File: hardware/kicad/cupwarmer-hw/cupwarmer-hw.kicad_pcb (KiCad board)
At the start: 4 copper layers, 56 x 56 mm, 50 parts, among them J1 I2C Service, J3 STATUS_MON, Q1 AO3400 SOT-23, U1 STWLC38JRM

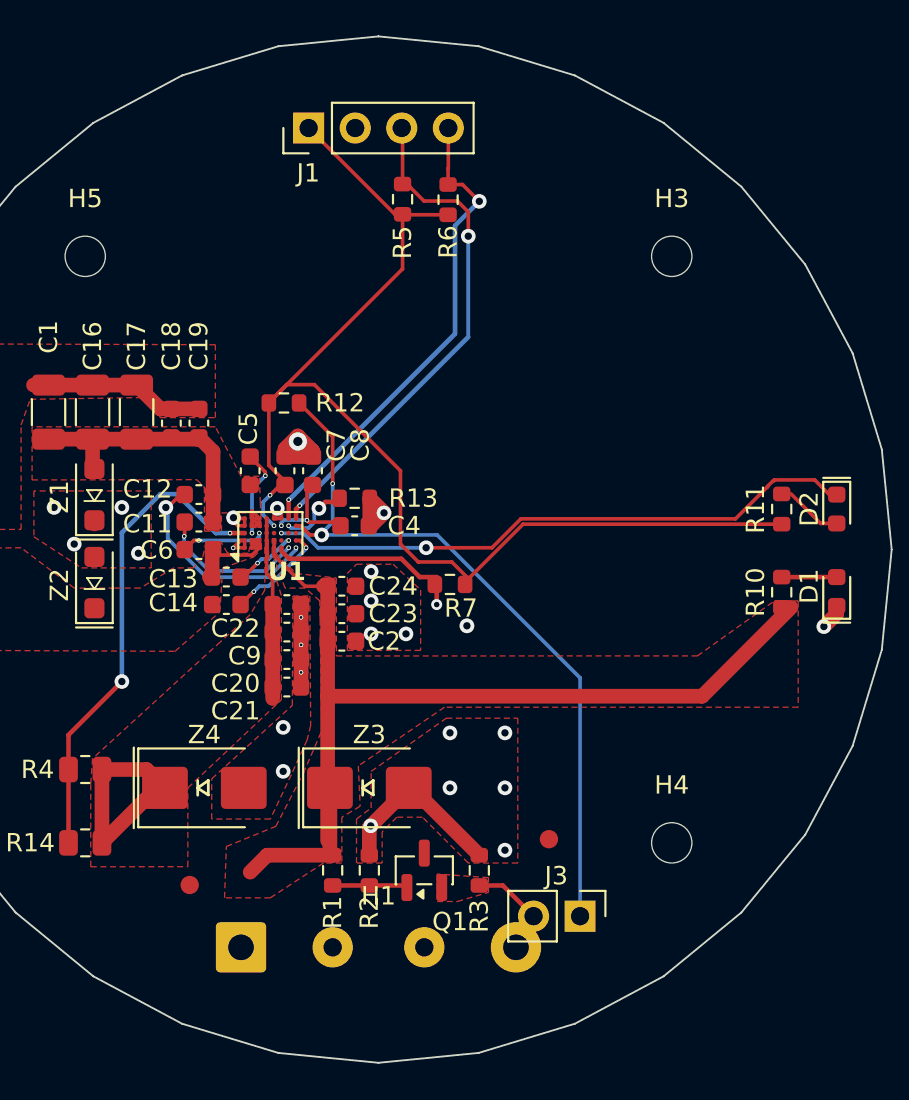
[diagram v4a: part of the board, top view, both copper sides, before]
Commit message: Refresh PCB footprint placements and TP1 land
Re-place and rotate several footprints (R1/R2/R3/R5/R6/R7, J1, H1, Q1)
to tidy reference text against the current layout, swap TP1 (TP_NTC)
from an SMD test pad to a 1x01 pin-header land for probe access, and
bump the default pad-mask drill/size in the project to 1.0/1.7 mm.

Co-Authored-By: Claude Opus 4.7 (1M context) <noreply@anthropic.com>
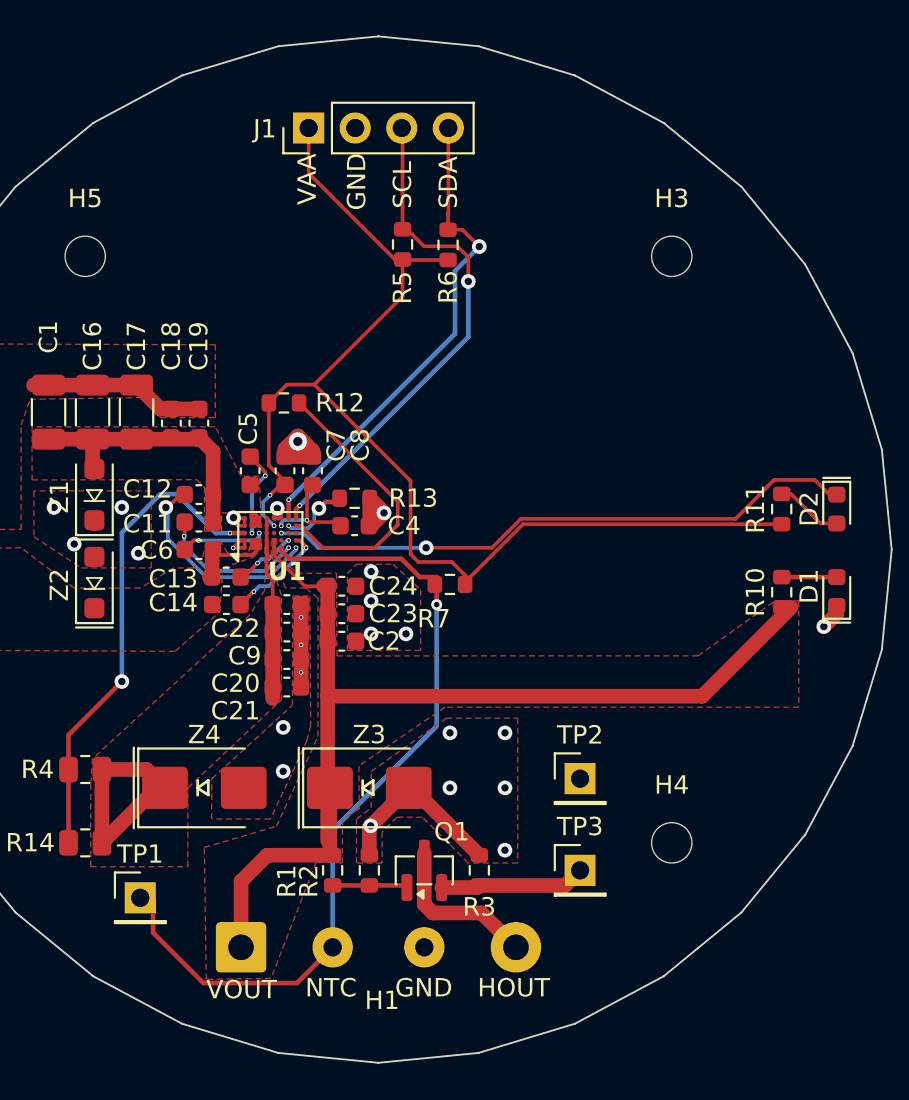
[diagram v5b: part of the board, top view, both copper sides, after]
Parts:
- removed J3: STATUS_MON, Connector_PinHeader_2.54mm:PinHeader_1x02_P2.54mm_Vertical
- added TP3: TP_I_HEATER_MON, Connector_PinHeader_2.54mm:PinHeader_1x01_P2.54mm_Vertical, F.Cu at (111.0, 117.5)
- TP1, TP2: footprint cupwarmer:TestPoint_Pad_D1.0mm_NoSilk -> Connector_PinHeader_2.54mm:PinHeader_1x01_P2.54mm_Vertical
- moved TP2 3.71 mm to (111.0, 112.5)
- moved TP1 2.79 mm to (87.0, 119.0)
- moved R5 2.47 mm to (101.3, 83.4)
- moved R6 2.47 mm to (103.8, 83.4)
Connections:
- net RX_INTB renamed Net-(U1-INTB)
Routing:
- net RX_NTC: track 10.7 -> 45.3 mm
- net Net-(U1-INTB): track 40.3 -> 15.6 mm, vias 2 -> 0
- net /heater-control/HEATER_OUT: track 0.00 -> 8.77 mm
- net VOUT_12V: track 55.1 -> 59.4 mm
- net I_HEATER_MON: track 3.99 -> 8.12 mm
- net RX_VAA: track 67.1 -> 65.1 mm, vias 3 -> 2
- removed copper zone on F.Cu, net I_HEATER_MON
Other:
- board text added: "GND"
- board text added: "HOUT"
- board text added: "NTC"
- board text added: "SCL"
- board text added: "SDA"
- board text added: "VAA"
- board text added: "VOUT"

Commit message: Add B.Cu SYS_GND pour and exclude H1/L1 wire pads from BOM/POS
- Add SYS_GND zone to B.Cu (full board polygon, fill params matching
  In1.Cu/In2.Cu GND pours) so the back-side signal layer carries a GND
  plane for return currents and EMI shielding.
- Mark H1 (heater harness) and L1 (Wuerth coil) as
  exclude_from_pos_files / exclude_from_bom in both the PCB instances
  and the cupwarmer.pretty library footprints. They are hand-soldered
  wire pads and should not appear in JLCPCB Pick&Place / BOM outputs.

DRC: 0 violations / 0 unconnected after refill_zones.

Plan: docs/plans/20260509-pcb-dual-review-fixes.md (Phase 2-1, 2-2, 3-2).

Co-Authored-By: Claude Opus 4.7 (1M context) <noreply@anthropic.com>
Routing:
- added copper zone on B.Cu, net SYS_GND
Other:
- board text added: "HTR_OUT"
- board text removed: "HOUT"
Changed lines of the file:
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@@
 		(tags "connector wire heater harness ntc")
 		(property "Reference" "H1"
-			(at 7.7 2.9 0)
+			(at 7.6 2.9 0)
 			(layer "F.SilkS")
 			(effects
@@
 			)
 		)
+		(attr through_hole exclude_from_pos_files exclude_from_bom)
 		(duplicate_pad_numbers_are_jumpers no)
 		(fp_rect
@@
 			)
 		)
+		(attr through_hole exclude_from_pos_files exclude_from_bom)
 		(duplicate_pad_numbers_are_jumpers no)
 		(fp_line
@@
 	)
 	(gr_text "NTC"
-		(at 96 124.5 0)
+		(at 96 124.6 0)
 		(layer "F.SilkS")
 		(effects
@@
 	)
 	(gr_text "GND"
-		(at 100.9 124.5 0)
+		(at 100.9 124.6 0)
 		(layer "F.SilkS")
 		(effects
@@
 		)
 	)
-	(gr_text "HOUT"
-		(at 105.4 124.5 0)
+	(gr_text "HTR_OUT"
+		(at 104.3 124.6 0)
 		(layer "F.SilkS")
 		(effects
@@
 	)
 	(segment
+		(start 97.5 121.7)
+		(end 95.55 123.65)
+		(width 0.25)
+		(layer "F.Cu")
+		(net "RX_NTC")
+	)
+	(segment
+		(start 95.55 123.65)
+		(end 90.45 123.65)
+		(width 0.25)
+		(layer "F.Cu")
+		(net "RX_NTC")
+	)
+	(segment
+		(start 95.123224 100.5)
+		(end 101.25 100.5)
+		(width 0.25)
+		(layer "F.Cu")
+		(net "RX_NTC")
+	)
+	(segment
+		(start 94.7 99.9)
+		(end 94.7 100.076776)
+		(width 0.25)
+		(layer "F.Cu")
+		(net "RX_NTC")
+	)
+	(segment
+		(start 103.175 101.5)
+		(end 103.175 103)
+		(width 0.25)
+		(layer "F.Cu")
+		(net "RX_NTC")
+	)
+	(segment
+		(start 103.175 101.5)
+		(end 102.25 101.5)
+		(width 0.25)
+		(layer "F.Cu")
+		(net "RX_NTC")
+	)
+	(segment
+		(start 90.45 123.65)
+		(end 87.7 120.9)
+		(width 0.25)
+		(layer "F.Cu")
+		(net "RX_NTC")
+	)
+	(segment
+		(start 102.25 101.5)
+		(end 101.25 100.5)
+		(width 0.25)
+		(layer "F.Cu")
+		(net "RX_NTC")
+	)
+	(segment
+		(start 94.7 100.076776)
+		(end 95.123224 100.5)
+		(width 0.25)
+		(layer "F.Cu")
+		(net "RX_NTC")
+	)
+	(segment
+		(start 87.7 120.9)
+		(end 87.7 119.1)
+		(width 0.25)
+		(layer "F.Cu")
+		(net "RX_NTC")
+	)
+	(via
+		(at 103.175 103)
+		(size 0.6)
+		(drill 0.3)
+		(layers "F.Cu" "B.Cu")
+		(net "RX_NTC")
+	)
+	(segment
+		(start 97.5 115.303984)
+		(end 103.175 109.628984)
+		(width 0.25)
+		(layer "B.Cu")
+		(net "RX_NTC")
+	)
+	(segment
+		(start 103.175 109.628984)
+		(end 103.175 103)
+		(width 0.25)
+		(layer "B.Cu")
+		(net "RX_NTC")
+	)
+	(segment
+		(start 97.5 121.7)
+		(end 97.5 115.303984)
+		(width 0.25)
+		(layer "B.Cu")
+		(net "RX_NTC")
+	)
+	(segment
 		(start 103.796779 81.670537)
 		(end 103.81 81.657316)
@@
 	)
 	(segment
-		(start 97.5 121.7)
-		(end 95.55 123.65)
-		(width 0.25)
-		(layer "F.Cu")
-		(net "RX_NTC")
-	)
-	(segment
-		(start 95.55 123.65)
-		(end 90.45 123.65)
-		(width 0.25)
-		(layer "F.Cu")
-		(net "RX_NTC")
-	)
-	(segment
-		(start 95.123224 100.5)
-		(end 101.25 100.5)
-		(width 0.25)
-		(layer "F.Cu")
-		(net "RX_NTC")
-	)
-	(segment
-		(start 94.7 99.9)
-		(end 94.7 100.076776)
-		(width 0.25)
-		(layer "F.Cu")
-		(net "RX_NTC")
-	)
-	(segment
-		(start 103.175 101.5)
-		(end 103.175 103)
-		(width 0.25)
-		(layer "F.Cu")
-		(net "RX_NTC")
-	)
-	(segment
-		(start 103.175 101.5)
-		(end 102.25 101.5)
-		(width 0.25)
-		(layer "F.Cu")
-		(net "RX_NTC")
-	)
-	(segment
-		(start 90.45 123.65)
-		(end 87.7 120.9)
-		(width 0.25)
-		(layer "F.Cu")
-		(net "RX_NTC")
-	)
-	(segment
-		(start 102.25 101.5)
-		(end 101.25 100.5)
-		(width 0.25)
-		(layer "F.Cu")
-		(net "RX_NTC")
-	)
-	(segment
-		(start 94.7 100.076776)
-		(end 95.123224 100.5)
-		(width 0.25)
-		(layer "F.Cu")
-		(net "RX_NTC")
-	)
-	(segment
-		(start 87.7 120.9)
-		(end 87.7 119.1)
-		(width 0.25)
-		(layer "F.Cu")
-		(net "RX_NTC")
-	)
-	(via
-		(at 103.175 103)
-		(size 0.6)
-		(drill 0.3)
-		(layers "F.Cu" "B.Cu")
-		(net "RX_NTC")
-	)
-	(segment
-		(start 97.5 115.303984)
-		(end 103.175 109.628984)
-		(width 0.25)
-		(layer "B.Cu")
-		(net "RX_NTC")
-	)
-	(segment
-		(start 103.175 109.628984)
-		(end 103.175 103)
-		(width 0.25)
-		(layer "B.Cu")
-		(net "RX_NTC")
-	)
-	(segment
-		(start 97.5 121.7)
-		(end 97.5 115.303984)
-		(width 0.25)
-		(layer "B.Cu")
-		(net "RX_NTC")
-	)
-	(segment
 		(start 105.625 119.825)
 		(end 107.5 121.7)
@@
 			)
 		)
+	)
+	(zone
+		(net "SYS_GND")
+		(layer "B.Cu")
+		(name "SYS_GND_BCu")
+		(hatch edge 0.5)
+		(connect_pads
+			(clearance 0.5)
+		)
+		(min_thickness 0.25)
+		(fill yes
+			(thermal_gap 0.5)
+			(thermal_bridge_width 0.5)
+			(island_removal_mode 0)
+		)
+		(polygon
+			(pts
+				(xy 70 70) (xy 130 70) (xy 130 130) (xy 70 130)
+			)
+		)

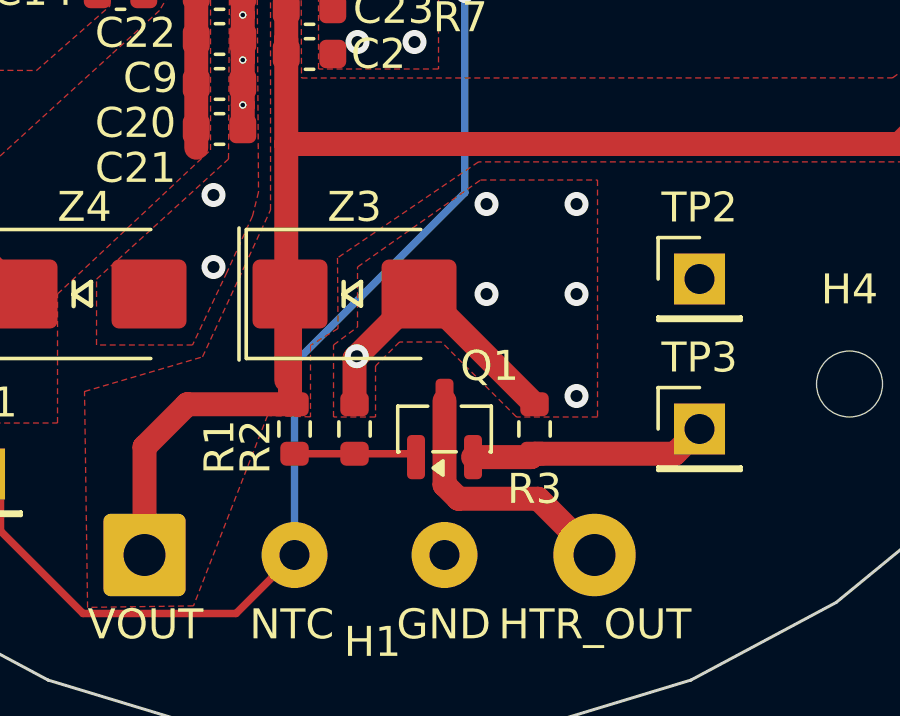
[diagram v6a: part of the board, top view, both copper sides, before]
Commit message: Upgrade R3 shunt footprint from 0603 to 1206 for 0.05R bring-up
Phase 3-3 of docs/plans/20260509-pcb-dual-review-fixes.md.

R3 sits in the heater current path: 0R for production, 0.05R during
bring-up to read I_HEATER_MON on a scope. At 1.4 A peak, 0.05R
dissipates ~100 mW, which has zero margin in 0603 (1/10 W). 1206 gives
4x derating and accommodates a dedicated current-sense part with a
useful TC.

- heater-control.kicad_sch: R3 footprint -> R_1206_3216Metric;
  production LCSC C17888 (1206W4F0000T5E, 0R 1206 Basic);
  Description annotates bring-up MPN FRM121WFR050TM (LCSC C7467249,
  1W 1206 +/-1% +/-50ppm) sourced from JLCPCB.
- cupwarmer-hw.kicad_pcb: pcb sync swapped R3 to 1206 footprint;
  manual reroute of HEATER_OUT and Q1 reference field done in KiCad
  to clear the larger 1206 pads. DRC: 0 errors / 0 unconnected
  (1 lib_footprint_mismatch warning, benign local override).

Co-Authored-By: Claude Opus 4.7 (1M context) <noreply@anthropic.com>
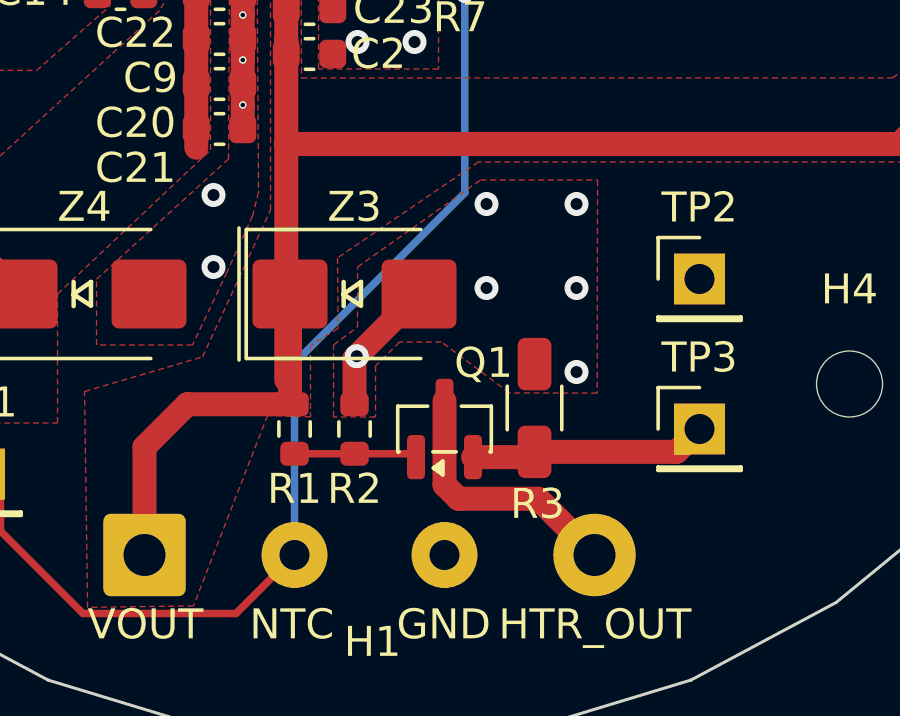
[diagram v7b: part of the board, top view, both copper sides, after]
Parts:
- R3: footprint Resistor_SMD:R_0603_1608Metric -> Resistor_SMD:R_1206_3216Metric
- moved R3 0.70 mm to (105.5, 116.8)
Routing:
- net SYS_GND: track 31.6 -> 26.4 mm
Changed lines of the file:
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@@
 	(property "PROJECT_NAME" "cupwarmer-hw")
 	(property "RX_IC" "STWLC38JRM")
-	(footprint "Resistor_SMD:R_0603_1608Metric"
-		(placed yes)
-		(layer "F.Cu")
-		(at 105.5 117.5 -90)
-		(descr "Resistor SMD 0603 (1608 Metric), square (rectangular) end terminal, IPC-7351 nominal, (Body size source: IPC-SM-782 page 72, https://www.pcb-3d.com/wordpress/wp-content/uploads/ipc-sm-782a_amendment_1_and_2.pdf)")
-		(tags "resistor")
-		(property "Reference" "R3"
-			(at 2 0 180)
-			(layer "F.SilkS")
-			(effects
-				(font
-					(size 1 1)
-					(thickness 0.15)
-				)
-			)
-		)
-		(property "Value" "0R/0.05R"
-			(at 0 1.43 90)
-			(layer "F.Fab")
-			(effects
-				(font
-					(size 1 1)
-					(thickness 0.15)
-				)
-			)
-		)
-		(property "Datasheet" "~"
-			(at 0 0 90)
-			(layer "F.Fab")
-			(hide yes)
-			(effects
-				(font
-					(size 1.27 1.27)
-				)
-			)
-		)
-		(property "Description" "Fit 0R for v1 normal build; substitute 0.05R for measured bring-up"
-			(at 0 0 90)
-			(layer "F.Fab")
-			(hide yes)
-			(effects
-				(font
-					(size 1.27 1.27)
-				)
-			)
-		)
-		(property "KiLib_Generator" "SMD_2terminal_chip_molded"
-			(at 0 0 90)
-			(layer "F.SilkS")
-			(hide yes)
-			(effects
-				(font
-					(size 1 1)
-					(thickness 0.15)
-				)
-			)
-		)
-		(property "Manufacturer" "UNI-ROYAL"
-			(at 0 0 270)
-			(unlocked yes)
-			(layer "F.Fab")
-			(hide yes)
-			(effects
-				(font
-					(size 1 1)
-					(thickness 0.15)
-				)
-			)
-		)
-		(property "LCSC" "C21189"
-			(at 0 0 270)
-			(unlocked yes)
-			(layer "F.Fab")
-			(hide yes)
-			(effects
-				(font
-					(size 1 1)
-					(thickness 0.15)
-				)
-			)
-		)
-		(property "MPN" "0603WAF0000T5E"
-			(at 0 0 270)
-			(unlocked yes)
-			(layer "F.Fab")
-			(hide yes)
-			(effects
-				(font
-					(size 1 1)
-					(thickness 0.15)
-				)
-			)
-		)
-		(sheetname "/heater-control/")
-		(sheetfile "heater-control.kicad_sch")
-		(units
-			(unit
-				(name "A")
-				(pins "1" "2")
-			)
-		)
-		(attr smd)
-		(duplicate_pad_numbers_are_jumpers no)
-		(fp_line
-			(start -0.237258 0.5225)
-			(end 0.237258 0.5225)
-			(stroke
-				(width 0.12)
-				(type solid)
-			)
-			(layer "F.SilkS")
-		)
-		(fp_line
-			(start -0.237258 -0.5225)
-			(end 0.237258 -0.5225)
-			(stroke
-				(width 0.12)
-				(type solid)
-			)
-			(layer "F.SilkS")
-		)
-		(fp_rect
-			(start -1.48 -0.73)
-			(end 1.48 0.73)
-			(stroke
-				(width 0.05)
-				(type solid)
-			)
-			(fill no)
-			(layer "F.CrtYd")
-		)
-		(fp_rect
-			(start -0.8 -0.4125)
-			(end 0.8 0.4125)
-			(stroke
-				(width 0.1)
-				(type solid)
-			)
-			(fill no)
-			(layer "F.Fab")
-		)
-		(fp_text user "${REFERENCE}"
-			(at 0 0 90)
-			(layer "F.Fab")
-			(effects
-				(font
-					(size 0.4 0.4)
-					(thickness 0.06)
-				)
-			)
-		)
-		(pad "1" smd roundrect
-			(at -0.825 0 270)
-			(size 0.8 0.95)
-			(layers "F.Cu" "F.Mask" "F.Paste")
-			(roundrect_rratio 0.25)
-			(net "SYS_GND")
-			(pinfunction "1_1")
-			(pintype "passive")
-		)
-		(pad "2" smd roundrect
-			(at 0.825 0 270)
-			(size 0.8 0.95)
-			(layers "F.Cu" "F.Mask" "F.Paste")
-			(roundrect_rratio 0.25)
-			(net "I_HEATER_MON")
-			(pinfunction "2_2")
-			(pintype "passive")
-		)
-		(embedded_fonts no)
-		(model "${KICAD10_3DMODEL_DIR}/Resistor_SMD.3dshapes/R_0603_1608Metric.step"
-			(offset
-				(xyz 0 0 0)
-			)
-			(scale
-				(xyz 1 1 1)
-			)
-			(rotate
-				(xyz 0 0 0)
-			)
-		)
-	)
 	(footprint "MountingHole:MountingHole_2.2mm_M2"
 		(layer "F.Cu")
@@
 		(tags "resistor")
 		(property "Reference" "R2"
-			(at 0.6 3.3 90)
+			(at 2 0 180)
 			(layer "F.SilkS")
 			(effects
@@
 		(tags "resistor")
 		(property "Reference" "R1"
-			(at 0.6 2.5 90)
+			(at 2 0 180)
 			(layer "F.SilkS")
 			(effects
@@
 		(tags "SOT TO_SOT_SMD")
 		(property "Reference" "Q1"
-			(at 2.1 1.5 180)
+			(at 2.2 1.3 180)
 			(layer "F.SilkS")
 			(effects
@@
 		)
 	)
+	(footprint "Resistor_SMD:R_1206_3216Metric"
+		(layer "F.Cu")
+		(at 105.5 116.8 -90)
+		(descr "Resistor SMD 1206 (3216 Metric), square (rectangular) end terminal, IPC-7351 nominal, (Body size source: IPC-SM-782 page 72, https://www.pcb-3d.com/wordpress/wp-content/uploads/ipc-sm-782a_amendment_1_and_2.pdf)")
+		(tags "resistor")
+		(property "Reference" "R3"
+			(at 3.2 -0.1 0)
+			(layer "F.SilkS")
+			(effects
+				(font
+					(size 1 1)
+					(thickness 0.15)
+				)
+			)
+		)
+		(property "Value" "0R/0.05R"
+			(at 0 1.83 0)
+			(layer "F.Fab")
+			(effects
+				(font
+					(size 1 1)
+					(thickness 0.15)
+				)
+			)
+		)
+		(property "Datasheet" ""
+			(at 0 0 270)
+			(layer "F.Fab")
+			(hide yes)
+			(effects
+				(font
+					(size 1.27 1.27)
+				)
+			)
+		)
+		(property "Description" ""
+			(at 0 0 270)
+			(layer "F.Fab")
+			(hide yes)
+			(effects
+				(font
+					(size 1.27 1.27)
+				)
+			)
+		)
+		(property "KiLib_Generator" "SMD_2terminal_chip_molded"
+			(at 0 0 0)
+			(layer "F.SilkS")
+			(hide yes)
+			(effects
+				(font
+					(size 1 1)
+					(thickness 0.15)
+				)
+			)
+		)
+		(attr smd)
+		(duplicate_pad_numbers_are_jumpers no)
+		(fp_line
+			(start -0.727064 0.91)
+			(end 0.727064 0.91)
+			(stroke
+				(width 0.12)
+				(type solid)
+			)
+			(layer "F.SilkS")
+		)
+		(fp_line
+			(start -0.727064 -0.91)
+			(end 0.727064 -0.91)
+			(stroke
+				(width 0.12)
+				(type solid)
+			)
+			(layer "F.SilkS")
+		)
+		(fp_rect
+			(start -2.28 -1.13)
+			(end 2.28 1.13)
+			(stroke
+				(width 0.05)
+				(type solid)
+			)
+			(fill no)
+			(layer "F.CrtYd")
+		)
+		(fp_rect
+			(start -1.6 -0.8)
+			(end 1.6 0.8)
+			(stroke
+				(width 0.1)
+				(type solid)
+			)
+			(fill no)
+			(layer "F.Fab")
+		)
+		(fp_text user "${REFERENCE}"
+			(at 0 0 0)
+			(layer "F.Fab")
+			(effects
+				(font
+					(size 0.8 0.8)
+					(thickness 0.12)
+				)
+			)
+		)
+		(pad "1" smd roundrect
+			(at -1.4625 0)
+			(size 1.125 1.75)
+			(layers "F.Cu" "F.Mask" "F.Paste")
+			(roundrect_rratio 0.222222)
+			(net "SYS_GND")
+		)
+		(pad "2" smd roundrect
+			(at 1.4625 0)
+			(size 1.125 1.75)
+			(layers "F.Cu" "F.Mask" "F.Paste")
+			(roundrect_rratio 0.222222)
+			(net "I_HEATER_MON")
+		)
+		(embedded_fonts no)
+		(model "${KICAD10_3DMODEL_DIR}/Resistor_SMD.3dshapes/R_1206_3216Metric.step"
+			(offset
+				(xyz 0 0 0)
+			)
+			(scale
+				(xyz 1 1 1)
+			)
+			(rotate
+				(xyz 0 0 0)
+			)
+		)
+	)
 	(footprint "Capacitor_SMD:C_0603_1608Metric"
 		(placed yes)
@@
 	)
 	(segment
-		(start 101.825 113)
-		(end 105.5 116.675)
-		(width 0.8)
-		(layer "F.Cu")
-		(net "SYS_GND")
-	)
-	(segment
 		(start 96.4 94.925)
 		(end 96.4 94.6)
@@
 	)
 	(via
-		(at 106.9 113)
+		(at 106.9 112.8)
 		(size 0.8)
 		(drill 0.4)
@@
 	)
 	(via
-		(at 106.9 116.4)
+		(at 106.9 115.6)
 		(size 0.8)
 		(drill 0.4)
@@
 	)
 	(via
-		(at 103.9 113)
+		(at 103.9 112.8)
 		(size 0.8)
 		(drill 0.4)
@@
 	)
 	(segment
-		(start 111 117.5)
-		(end 110.175 118.325)
-		(width 0.8)
+		(start 105.375 118.45)
+		(end 105.5 118.325)
+		(width 0.25)
 		(layer "F.Cu")
 		(net "I_HEATER_MON")
 	)
 	(segment
-		(start 105.375 118.45)
-		(end 105.5 118.325)
-		(width 0.25)
+		(start 105.325 118.4375)
+		(end 105.5 118.2625)
+		(width 0.8)
 		(layer "F.Cu")
 		(net "I_HEATER_MON")
@@
 	(segment
 		(start 103.45 118.4375)
-		(end 105.3875 118.4375)
+		(end 105.325 118.4375)
 		(width 0.8)
 		(layer "F.Cu")
@@
 	)
 	(segment
-		(start 110.175 118.325)
-		(end 105.5 118.325)
+		(start 110.2375 118.2625)
+		(end 111 117.5)
 		(width 0.8)
 		(layer "F.Cu")
@@
 	)
 	(segment
-		(start 105.3875 118.4375)
-		(end 105.5 118.325)
+		(start 105.5 118.2625)
+		(end 110.2375 118.2625)
 		(width 0.8)
 		(layer "F.Cu")
@@
 			(pts
 				(xy 98.8 117.1) (xy 98.8 114.7) (xy 99.6 114.1) (xy 99.6 112.1) (xy 103.7 109.2) (xy 107.6 109.2)
-				(xy 107.6 117.1) (xy 104.9 117.1) (xy 102.4 114.6) (xy 101 114.6) (xy 100.2 115.4) (xy 100.2 117.1)
+				(xy 107.587374 116.302645) (xy 104.663261 116.297446) (xy 102.4 114.6) (xy 101 114.6) (xy 100.2 115.4)
+				(xy 100.2 117.1)
 			)
 		)
